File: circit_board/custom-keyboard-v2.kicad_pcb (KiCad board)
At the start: 2 copper layers, 266 x 99.8 mm, 140 parts, among them J1 i2c_display, SW1 SW_Push, SW10 SW_Push, SW11 SW_Push, SW12 SW_Push, SW13 SW_Push, SW14 SW_Push, SW15 SW_Push, SW16 SW_Push, SW17 SW_Push, SW18 SW_Push, SW19 SW_Push, SW2 SW_Push, SW20 SW_Push, SW21 SW_Push, SW22 SW_Push, SW23 SW_Push, SW24 SW_Push, SW25 SW_Push, SW26 SW_Push, SW27 SW_Push, SW28 SW_Push, SW29 SW_Push, SW3 SW_Push, SW30 SW_Push, SW31 SW_Push, SW32 SW_Push, SW33 SW_Push, SW34 SW_Push, SW35 SW_Push, SW36 SW_Push, SW37 SW_Push, SW38 SW_Push, SW39 SW_Push, SW4 SW_Push, SW40 SW_Push, SW41 SW_Push, SW42 SW_Push, SW43 SW_Push, SW44 SW_Push, SW45 SW_Push, SW46 SW_Push, SW5 SW_Push, SW6 SW_Push, SW7 SW_Push, SW8 SW_Push, SW9 SW_Push

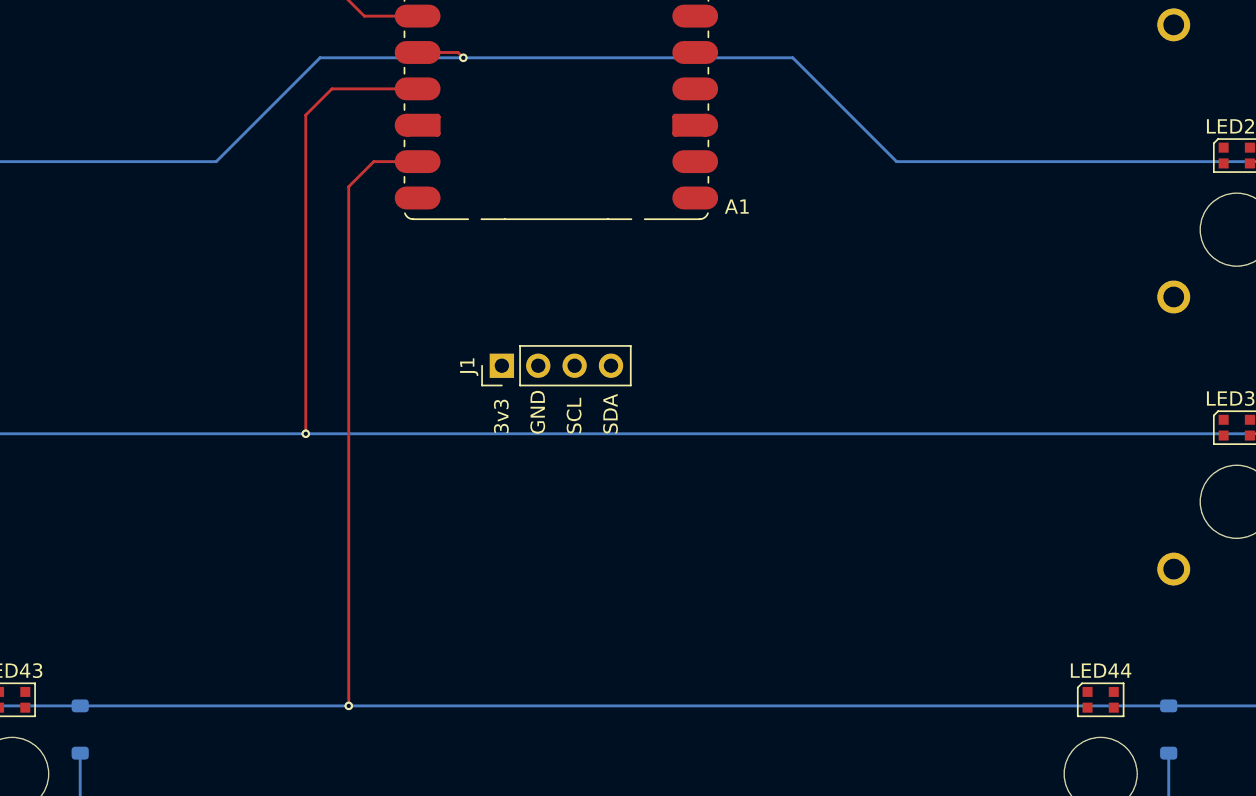
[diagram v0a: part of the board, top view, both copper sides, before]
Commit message: Added 3V -> 5V converter for LED data line
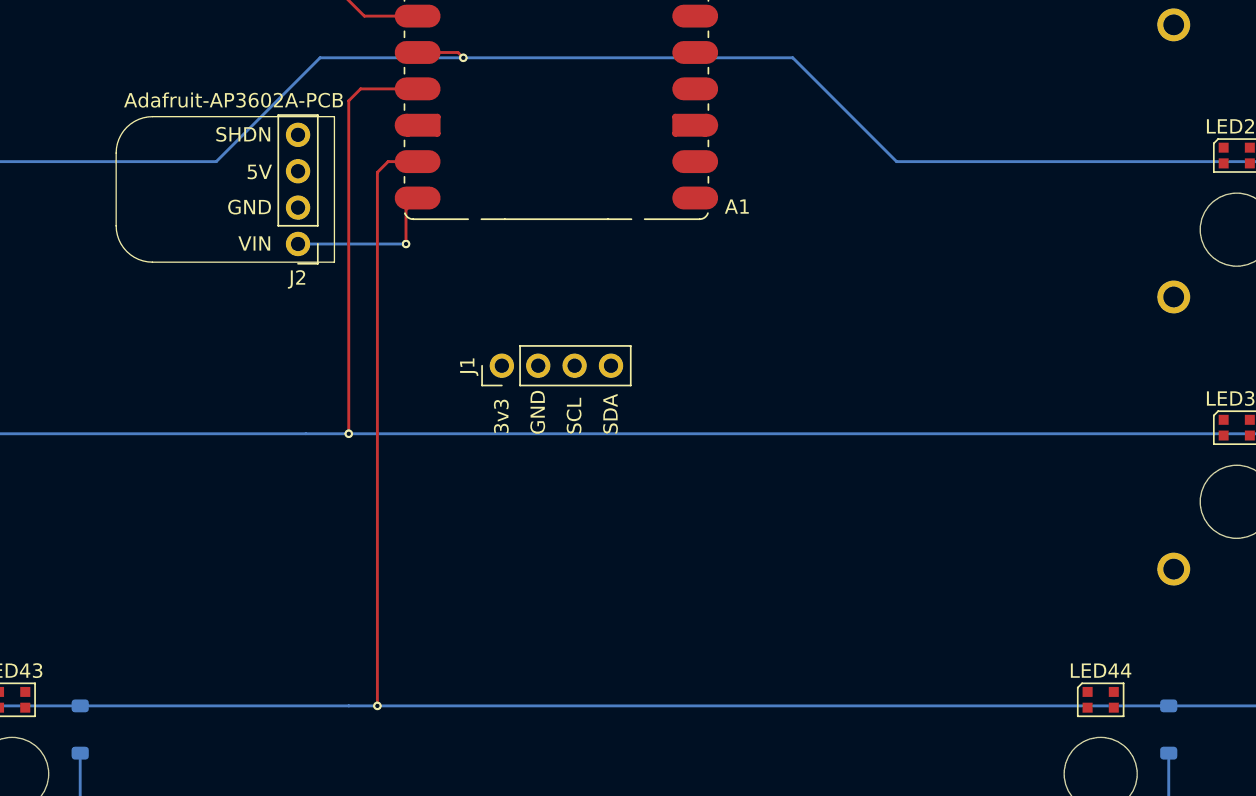
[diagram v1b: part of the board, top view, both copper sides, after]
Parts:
- added J2: Adafruit-AP3602A-PCB, Connector_PinHeader_2.54mm:PinHeader_1x04_P2.54mm_Vertical, F.Cu at (200.5, 134.0)
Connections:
- A1 pad 20: led-data -> Net-(A1-GPIO15)
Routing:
- net Net-(A1-GPIO15): track 0.00 -> 11.1 mm, vias 0 -> 1
- net row4: track 289.6 -> 287.2 mm
- net row5: track 193.8 -> 192.4 mm
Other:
- board text added: "5V"
- board text added: "SHDN"
- board text added: "VIN"

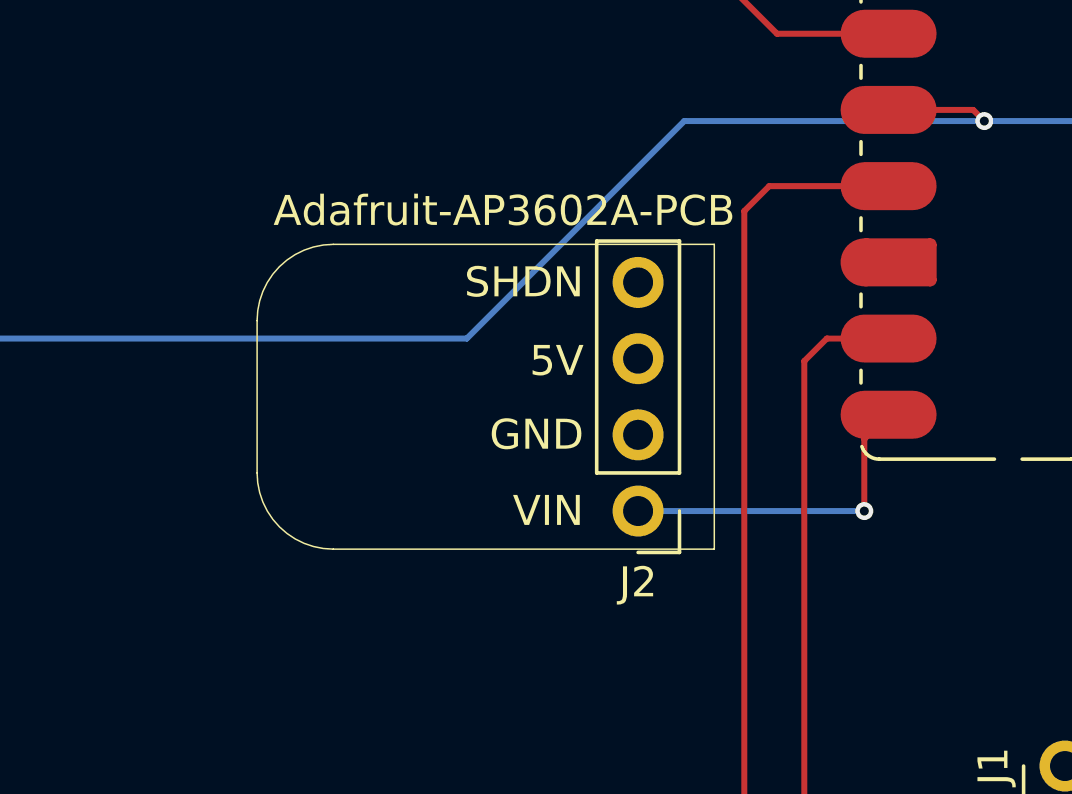
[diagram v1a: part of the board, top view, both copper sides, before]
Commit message: Swaped 3V -> 5V convert from through-hole to SMT pads
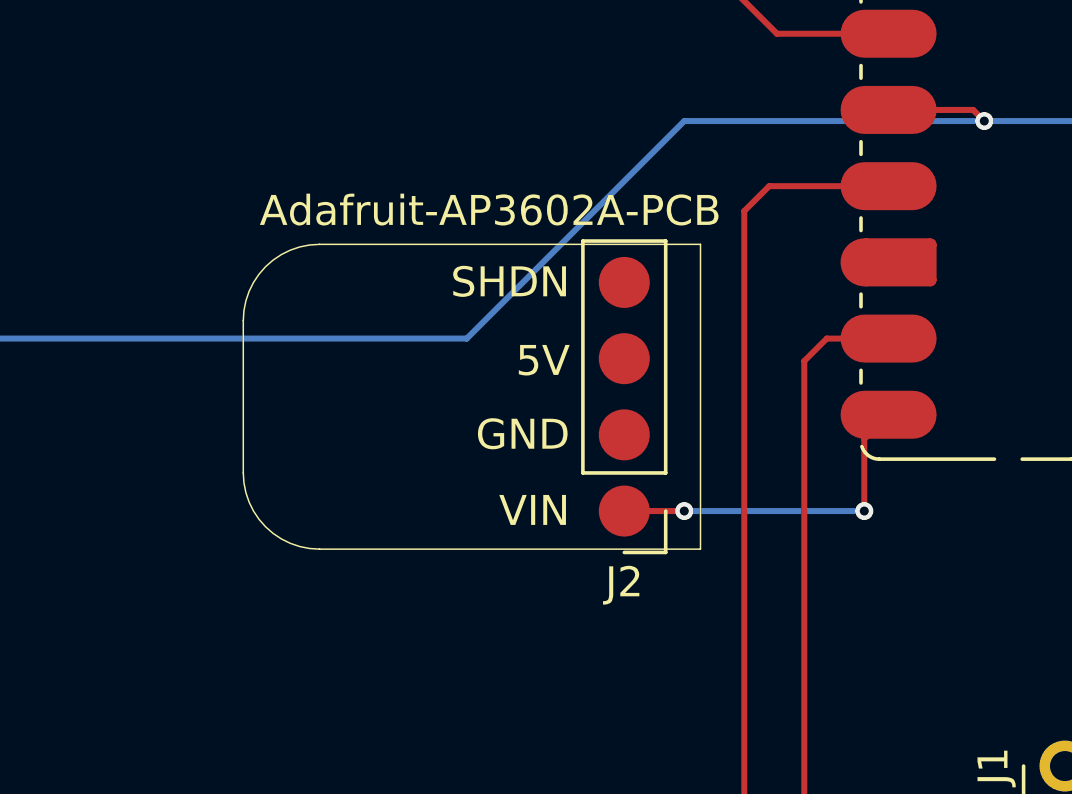
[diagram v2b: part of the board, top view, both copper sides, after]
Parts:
- moved J2 0.46 mm to (200.0, 134.0)
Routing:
- net Net-(A1-GPIO15): track 11.1 -> 11.5 mm, vias 1 -> 2
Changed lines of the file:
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@@
 	(footprint "Connector_PinHeader_2.54mm:PinHeader_1x04_P2.54mm_Vertical"
 		(layer "F.Cu")
-		(at 200.46 134 180)
+		(at 200 134 180)
 		(descr "Through hole straight pin header, 1x04, 2.54mm pitch, single row")
 		(tags "Through hole pin header THT 1x04 2.54mm single row")
@@
 			)
 		)
-		(pad "1" thru_hole circle
+		(pad "1" smd circle
 			(at 0 0 180)
 			(size 1.7 1.7)
-			(drill 1)
-			(layers "*.Cu" "*.Mask")
-			(remove_unused_layers no)
+			(layers "F.Cu" "F.Mask" "F.Paste")
 			(net 127 "Net-(A1-GPIO15)")
 			(pinfunction "Pin_1")
 			(pintype "passive")
 		)
-		(pad "2" thru_hole circle
+		(pad "2" smd circle
 			(at 0 2.54 180)
 			(size 1.7 1.7)
-			(drill 1)
-			(layers "*.Cu" "*.Mask")
-			(remove_unused_layers no)
+			(layers "F.Cu" "F.Mask" "F.Paste")
 			(net 18 "gnd")
 			(pinfunction "Pin_2")
 			(pintype "passive")
 		)
-		(pad "3" thru_hole circle
+		(pad "3" smd circle
 			(at 0 5.08 180)
 			(size 1.7 1.7)
-			(drill 1)
-			(layers "*.Cu" "*.Mask")
-			(remove_unused_layers no)
+			(layers "F.Cu" "F.Mask" "F.Paste")
 			(net 32 "led-data")
 			(pinfunction "Pin_3")
 			(pintype "passive")
 		)
-		(pad "4" thru_hole circle
+		(pad "4" smd circle
 			(at 0 7.62 180)
 			(size 1.7 1.7)
-			(drill 1)
-			(layers "*.Cu" "*.Mask")
-			(remove_unused_layers no)
+			(layers "F.Cu" "F.Mask" "F.Paste")
 			(net 128 "unconnected-(J2-Pin_4-Pad4)")
 			(pinfunction "Pin_4")
@@
 	)
 	(gr_arc
-		(start 190.3 135.27)
-		(mid 188.503949 134.526051)
-		(end 187.76 132.73)
+		(start 189.84 135.27)
+		(mid 188.043949 134.526051)
+		(end 187.3 132.73)
 		(stroke
 			(width 0.05)
@@
 	)
 	(gr_line
-		(start 203 135.27)
-		(end 190.3 135.27)
+		(start 202.54 135.27)
+		(end 189.84 135.27)
 		(stroke
 			(width 0.05)
@@
 	)
 	(gr_line
-		(start 203 125.11)
-		(end 203 135.27)
+		(start 202.54 125.11)
+		(end 202.54 135.27)
 		(stroke
 			(width 0.05)
@@
 	)
 	(gr_arc
-		(start 187.76 127.65)
-		(mid 188.503949 125.853949)
-		(end 190.3 125.11)
+		(start 187.3 127.65)
+		(mid 188.043949 125.853949)
+		(end 189.84 125.11)
 		(stroke
 			(width 0.05)
@@
 	)
 	(gr_line
-		(start 190.3 125.11)
-		(end 203 125.11)
+		(start 189.84 125.11)
+		(end 202.54 125.11)
 		(stroke
 			(width 0.05)
@@
 	)
 	(gr_line
-		(start 187.76 132.73)
-		(end 187.76 127.65)
+		(start 187.3 132.73)
+		(end 187.3 127.65)
 		(stroke
 			(width 0.05)
@@
 	)
 	(gr_text "5V\n"
-		(at 198.65 129 0)
+		(at 198.19 129 0)
 		(layer "F.SilkS")
 		(effects
@@
 	)
 	(gr_text "SHDN"
-		(at 198.65 126.38 0)
+		(at 198.19 126.38 0)
 		(layer "F.SilkS")
 		(effects
@@
 	)
 	(gr_text "VIN"
-		(at 198.65 134 0)
+		(at 198.19 134 0)
 		(layer "F.SilkS")
 		(effects
@@
 	)
 	(gr_text "GND"
-		(at 198.65 131.46 0)
+		(at 198.19 131.46 0)
 		(layer "F.SilkS")
 		(effects
@@
 	)
 	(segment
-		(start 208.81 130.79)
+		(start 208 134)
 		(end 208 131.6)
 		(width 0.2)
@@
 	)
 	(segment
+		(start 200 134)
+		(end 202 134)
+		(width 0.2)
+		(layer "F.Cu")
+		(net 127)
+	)
+	(segment
 		(start 208 131.6)
-		(end 208 134)
+		(end 208.81 130.79)
 		(width 0.2)
 		(layer "F.Cu")
@@
 	)
 	(via
+		(at 202 134)
+		(size 0.6)
+		(drill 0.3)
+		(layers "F.Cu" "B.Cu")
+		(net 127)
+	)
+	(via
 		(at 208 134)
 		(size 0.6)
@@
 	)
 	(segment
-		(start 208 134)
-		(end 200.46 134)
+		(start 202 134)
+		(end 208 134)
 		(width 0.2)
 		(layer "B.Cu")

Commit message: Key switch matrix fully routed
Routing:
- net col1: track 0.00 -> 194.1 mm, vias 0 -> 1
- net col10: track 0.00 -> 189.5 mm, vias 0 -> 1
- net col8: track 0.00 -> 179.8 mm, vias 0 -> 1
- net col3: track 0.00 -> 179.3 mm, vias 0 -> 2
- net col2: track 0.00 -> 173.5 mm, vias 0 -> 2
- net col9: track 0.00 -> 170.3 mm, vias 0 -> 1
- net col4: track 0.00 -> 160.1 mm, vias 0 -> 2
- net col7: track 0.00 -> 154.0 mm, vias 0 -> 1
- net col6: track 0.00 -> 136.3 mm, vias 0 -> 1
- net col5: track 0.00 -> 126.7 mm, vias 0 -> 1

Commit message: Added ground plane
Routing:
- added copper zone on B.Cu, net gnd
- added copper zone on F.Cu, net gnd
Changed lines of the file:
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@@
 		(net 127)
+	)
+	(zone
+		(net 18)
+		(net_name "gnd")
+		(layers "F.Cu" "B.Cu")
+		(hatch edge 0.5)
+		(connect_pads
+			(clearance 0.5)
+		)
+		(min_thickness 0.25)
+		(filled_areas_thickness no)
+		(fill yes
+			(thermal_gap 0.5)
+			(thermal_bridge_width 0.5)
+		)
+		(polygon
+			(pts
+				(xy 76 57) (xy 76 190) (xy 361 190) (xy 361 57)
+			)
+		)
 	)
 	(group ""

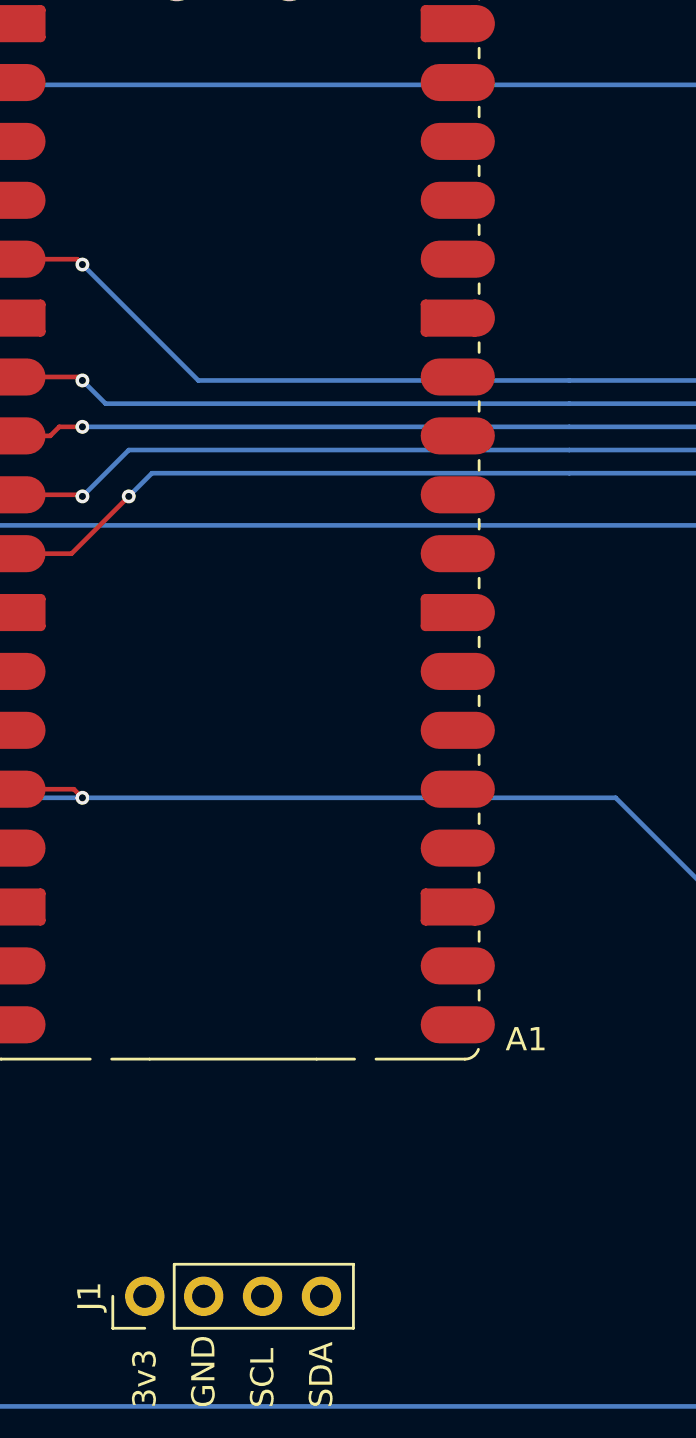
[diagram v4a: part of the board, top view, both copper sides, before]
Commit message: Wired up the OLED display
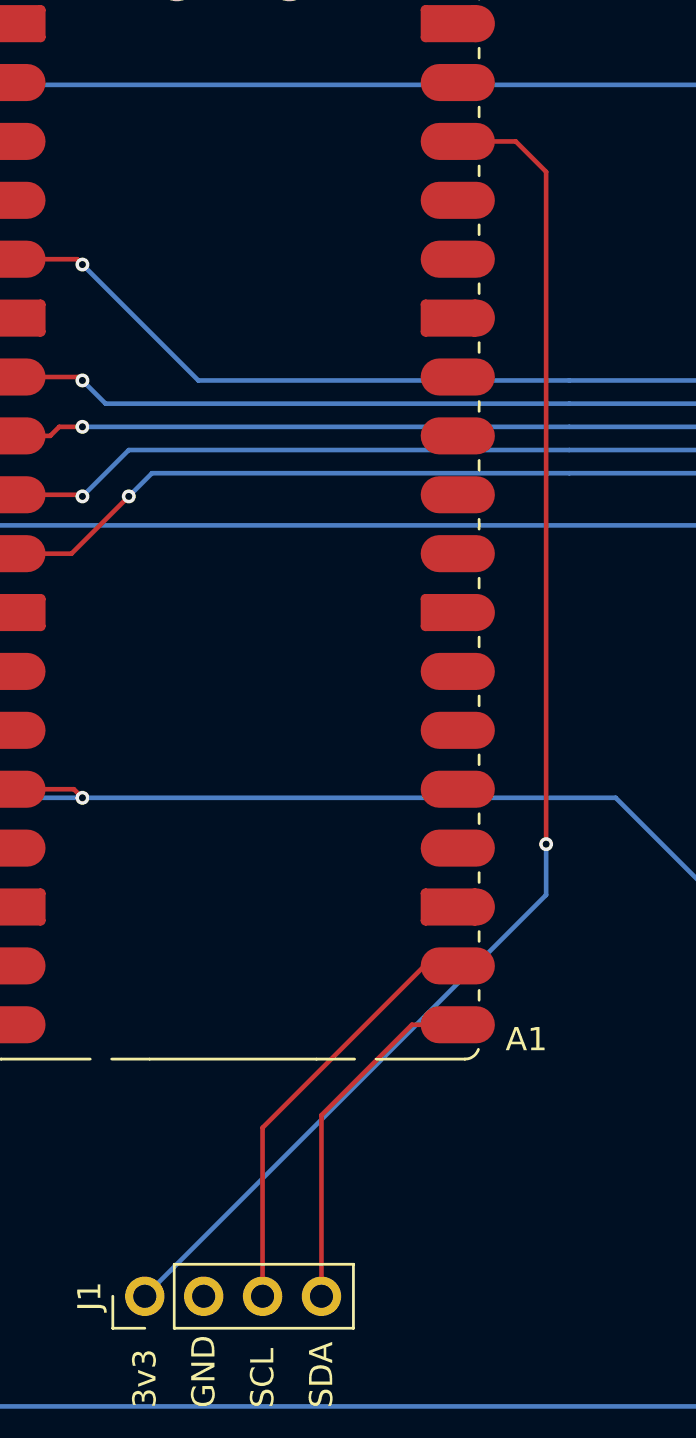
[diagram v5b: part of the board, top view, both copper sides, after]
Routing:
- net OLED-power: track 0.00 -> 60.0 mm, vias 0 -> 1
- net I2C-SCL: track 0.00 -> 18.6 mm
- net I2C-SDA: track 0.00 -> 15.3 mm
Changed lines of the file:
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@@
+	)
+	(segment
+		(start 226.21 130.79)
+		(end 222.31 134.69)
+		(width 0.2)
+		(layer "F.Cu")
+		(net 5)
+	)
+	(segment
+		(start 222.31 134.69)
+		(end 222.31 142.5)
+		(width 0.2)
+		(layer "F.Cu")
+		(net 5)
+	)
+	(segment
+		(start 228.19 130.79)
+		(end 226.21 130.79)
+		(width 0.2)
+		(layer "F.Cu")
+		(net 5)
+	)
+	(segment
+		(start 230.69 92.69)
+		(end 232 94)
+		(width 0.2)
+		(layer "F.Cu")
+		(net 11)
+	)
+	(segment
+		(start 228.19 92.69)
+		(end 230.69 92.69)
+		(width 0.2)
+		(layer "F.Cu")
+		(net 11)
+	)
+	(segment
+		(start 232 94)
+		(end 232 123)
+		(width 0.2)
+		(layer "F.Cu")
+		(net 11)
+	)
+	(via
+		(at 232 123)
+		(size 0.6)
+		(drill 0.3)
+		(layers "F.Cu" "B.Cu")
+		(net 11)
+	)
+	(segment
+		(start 232 125.19)
+		(end 214.69 142.5)
+		(width 0.2)
+		(layer "B.Cu")
+		(net 11)
+	)
+	(segment
+		(start 232 123)
+		(end 232 125.19)
+		(width 0.2)
+		(layer "B.Cu")
+		(net 11)
+	)
+	(segment
+		(start 228.19 128.25)
+		(end 226.75 128.25)
+		(width 0.2)
+		(layer "F.Cu")
+		(net 14)
+	)
+	(segment
+		(start 226.75 128.25)
+		(end 219.77 135.23)
+		(width 0.2)
+		(layer "F.Cu")
+		(net 14)
+	)
+	(segment
+		(start 219.77 135.23)
+		(end 219.77 142.5)
+		(width 0.2)
+		(layer "F.Cu")
+		(net 14)
 	)
 	(segment

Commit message: Connected LED chain data pins
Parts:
- moved LED10 209.2 mm to (133.0, 104.1)
- moved LED31 191.5 mm to (285.0, 127.8)
- moved LED8 190.1 mm to (114.0, 89.8)
- moved LED9 190.1 mm to (133.0, 85.1)
- moved LED41 184.5 mm to (323.0, 127.8)
- moved LED7 172.1 mm to (114.0, 108.8)
- moved LED20 171.1 mm to (171.0, 108.8)
- moved LED32 171.0 mm to (285.0, 146.8)
- moved LED42 162.6 mm to (323.0, 146.8)
- moved LED43 162.1 mm to (342.0, 151.6)
- moved LED6 156.7 mm to (114.0, 127.8)
- moved LED19 153.2 mm to (171.0, 89.8)
- moved LED18 152.7 mm to (152.0, 89.8)
- moved LED33 144.5 mm to (275.5, 165.8)
- moved LED34 143.8 mm to (294.5, 165.8)
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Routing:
- net Net-(LED23-DOUT): track 0.00 -> 95.2 mm
- net Net-(LED13-DOUT): track 0.00 -> 46.8 mm
- net Net-(LED42-DOUT): track 0.00 -> 46.5 mm
- net Net-(LED4-DOUT): track 0.00 -> 43.7 mm
- net Net-(LED33-DOUT): track 0.00 -> 37.8 mm
- net Net-(LED12-DOUT): track 0.00 -> 31.6 mm
- net Net-(LED22-DOUT): track 0.00 -> 29.1 mm
- net Net-(LED34-DOUT): track 0.00 -> 29.1 mm
- net Net-(LED18-DOUT): track 0.00 -> 28.5 mm
- net Net-(LED38-DOUT): track 0.00 -> 25.7 mm
- net Net-(LED8-DOUT): track 0.00 -> 24.9 mm
- net Net-(LED32-DOUT): track 0.00 -> 23.9 mm
- net Net-(LED40-DOUT): track 0.00 -> 23.2 mm
- net Net-(LED30-DOUT): track 0.00 -> 23.2 mm
- net Net-(LED11-DOUT): track 0.00 -> 23.2 mm
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
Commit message: Powered LEDs by flooding the back layer with copper
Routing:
- net led-power: track 0.00 -> 163.9 mm, vias 0 -> 66
- net led-data: track 0.00 -> 137.5 mm
- net gnd: track 0.00 -> 100.4 mm, vias 0 -> 52
- net Net-(LED18-DOUT): track 28.5 -> 22.7 mm
- net Net-(LED22-DOUT): track 29.1 -> 30.4 mm
- added copper zone on B.Cu, net led-power
- removed copper zone on B.Cu, net gnd
